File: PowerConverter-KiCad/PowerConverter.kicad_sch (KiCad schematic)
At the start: 47 parts, among them Q1 Q_NMOS_GDS, U1 UCC27517AQDBVRQ1, U2 STM32G431RBTx, U3 AP63205WU, U4 AMS1117-3.3, Y1 16MHz

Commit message: Şema ve BOM optimizasyonu tamamlandı. PCB Layout aşamasına geçiliyor.
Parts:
- removed D1: MBR1045, MBR1045CadModel:TO508P1050X476X2020-2, symbol MBR1045:MBR1045
- removed Q1: Q_NMOS_GDS, symbol Transistor_FET:Q_NMOS_GDS
- added C26, C28: 100nF, Capacitor_SMD:C_0603_1608Metric_Pad1.08x0.95mm_HandSolder, symbol Device:C
- added C27: 10uF, Capacitor_SMD:C_0805_2012Metric_Pad1.18x1.45mm_HandSolder, symbol Device:C
- added D1: PMEG060V100EPDZ, symbol Device:D_Schottky
- added Q1: IRFB7430PBF, symbol Simulation_SPICE:NMOS
- added R10: 10k, Resistor_SMD:R_0603_1608Metric_Pad0.98x0.95mm_HandSolder, symbol Device:R_US
- added TH1: Thermistor_NTC, Resistor_SMD:R_0603_1608Metric_Pad0.98x0.95mm_HandSolder, symbol Device:Thermistor_NTC
- C1: footprint (none) -> Capacitor_THT:CP_Radial_D16.0mm_P7.50mm
- C10, C14, C15, C16, C17, C21, C22, C23, C24, C25, C6, C7, C8: footprint (none) -> Capacitor_SMD:C_0603_1608Metric_Pad1.08x0.95mm_HandSolder
- C11, C12, C2, C9: footprint (none) -> Capacitor_SMD:C_1210_3225Metric_Pad1.33x2.70mm_HandSolder
- C13: footprint (none) -> Capacitor_Tantalum_SMD:CP_EIA-3528-21_Kemet-B_HandSolder
- C18, C19, C20, C4, C5: footprint (none) -> Capacitor_SMD:C_0805_2012Metric_Pad1.18x1.45mm_HandSolder
- C3: footprint (none) -> Capacitor_THT:CP_Radial_D8.0mm_P5.00mm
- D2: footprint (none) -> LED_SMD:LED_0805_2012Metric_Pad1.15x1.40mm_HandSolder
- L1, L2: value 47uH -> 10uH; footprint (none) -> Inductor_SMD:L_Bourns_SRP1245A
- L3: footprint (none) -> Inductor_SMD:L_Taiyo-Yuden_NR-30xx
- R1, R2, R4, R5, R7, R8, R9: footprint (none) -> Resistor_SMD:R_0603_1608Metric_Pad0.98x0.95mm_HandSolder
- R3: footprint (none) -> Resistor_SMD:R_2512_6332Metric_Pad1.40x3.35mm_HandSolder
- R6: footprint (none) -> Resistor_SMD:R_0805_2012Metric_Pad1.20x1.40mm_HandSolder
- U1: footprint DBV5_TEX -> footprints:DBV5_TEX
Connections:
- net +12V: now also C27.1, C28.1
- net +3.3V: now also R10.2
- net GND: now also C27.2, C28.2; no longer C5.2, C6.2, U1.2 (GND), U1.4 (IN-)
- net GNDA: now also C26.2, TH1.2
- net Gate: now also Q1.2 (G)
- net at C2.1, L1.2: now also Q1.1 (D)
- net Source: now reaches R3.1, R5.1
- net Source: now also C5.2, C6.2, U1.2 (GND), U1.4 (IN-), Q1.3 (S)
- net at C3.1, C4.1, R1.2: now also D1.1 (K)
- net at C2.2, L2.1: now also D1.2 (A)
- net PB2: now reaches U2.26 (PB2)
- net PB2: now also C26.1, R10.1, TH1.1
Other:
- moved on the sheet: C1, L1

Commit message: Layout: Buck ve LDO yerleşimi tamamlandı, sakin ada stratejisi uygulandı
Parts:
- added J1: 3220-10-0100-00, digikey-footprints:PinHeader_2x5_P1.27mm_Drill.7mm, symbol dk_Rectangular-Connectors-Headers-Male-Pins:3220-10-0100-00
- added J2: Conn_01x03_Pin, Connector_PinHeader_2.54mm:PinHeader_1x03_P2.54mm_Vertical, symbol Connector:Conn_01x03_Pin
- added R11: 10k, Resistor_SMD:R_0603_1608Metric_Pad0.98x0.95mm_HandSolder, symbol Device:R_US
- D1: footprint (none) -> Package_TO_SOT_SMD:TO-277B
- Q1: footprint (none) -> Package_TO_SOT_THT:TO-220-3_Vertical
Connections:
- net +3.3V: now also J1.1, J2.1 (Pin_1)
- net GND: now also J1.3, J1.5, J1.9, J2.3 (Pin_3); no longer R9.1
- net SWDCLK: now also J1.4
- net SWDIO: now also J1.2
- net V_O2: now reaches C3.1, C4.1, D1.1 (K), R1.2
- net V_O1: now reaches C2.2, D1.2 (A), L2.1
- net SW_NODE: now reaches C2.1, L1.2, Q1.1 (D)
- net BOOT0: now reaches R9.2, U2.61 (PB8)
- net at C24.2: now also R11.1; no longer U2.7 (PG10)
- net SWO: now reaches U2.56 (PB3)
- net SWO: now also J1.6
- new net: J2.2 (Pin_2), R9.1
- new net NRST: J1.10, R11.2, U2.7 (PG10)
- no-connect marks 0 -> 43
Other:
- note added: "STM32G4 serisinde bu jumper'ın çalışması için bir kereliğine yazılımsal bir ayar gerekebilir: nBOOT_SEL: Eğer Option Bytes içinde bu bit 1 ise, işlemci fiziksel BOOT0 pinini (senin bu jumper'ı) görmezden gelir. Çözüm: CubeIDE içindeki Programmer kısmından nBOOT_SEL bitini 0 yaparsan, işlemci artık tamamen senin bu fiziksel jumper'ının sözünü dinlemeye başlar."
- moved on the sheet: C24, C25

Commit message: SEPIC v2.0: 4-Layer Stackup, 12V Power Plane on In2, and High Current Via Stitching implemented
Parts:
- added D3, D4, D5, D6: BAT54S, Package_TO_SOT_SMD:SOT-23, symbol Diode:BAT54S
- added D7: SMAJ15A, Diode_SMD:D_SMC, symbol Diode:SMAJ15A
- added F1: Fuse, Fuse:Fuseholder_Cylinder-5x20mm_Wuerth_696103101002-SMD_Horizontal_Open, symbol Device:Fuse
- added H1, H2, H3, H4: MountingHole, MountingHole:MountingHole_3.2mm_M3, symbol Mechanical:MountingHole
- added J3, J4: Screw_Terminal_01x02, digikey-footprints:Term_Block_1x2_P5.08MM, symbol Connector:Screw_Terminal_01x02
- added R12, R13: 1k, Resistor_SMD:R_0603_1608Metric_Pad0.98x0.95mm_HandSolder, symbol Device:R_US
- R5: value 100 -> 1k
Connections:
- net +12V: now also F1.1, J3.2 (Pin_2); no longer C1.1, C27.1, C28.1, L1.1
- net +3.3VA: now also D3.2 (K), D4.2 (K), D5.2 (K), D6.2 (K)
- net GND: now also D7.2 (A2), J3.1 (Pin_1), J4.2 (Pin_2), R12.1
- net GNDA: now also D3.1 (A), D4.1 (A), D5.1 (A), D6.1 (A); no longer C8.2
- net PA1: now also D3.3 (COM)
- net PA7: now also D4.3 (COM); no longer C8.1, R5.2, U2.21 (PA7)
- net PB2: now also D5.3 (COM), R13.1; no longer C26.1, R10.1, TH1.1
- net V_O2: now also J4.1 (Pin_1)
- net I_SENSE_N: now reaches U2.19 (PA5)
- net I_SENSE_N: now also C8.2, R12.2
- new net: C26.1, R10.1, R13.2, TH1.1
- new net: C1.1, C27.1, C28.1, D7.1 (A1), F1.2, L1.1
- new net I_SENSE_P: C8.1, R5.2, U2.21 (PA7)
- new net PA5: D6.3 (COM)
- no-connect marks 43 -> 42
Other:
- moved on the sheet: C1, C2, C27, C28, C3, C4, C7, C8, D1, L1, L2, Q1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

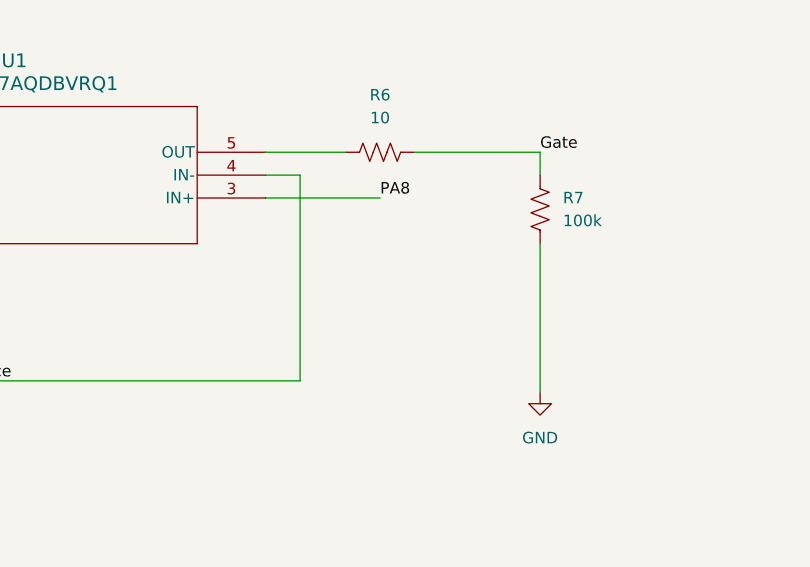
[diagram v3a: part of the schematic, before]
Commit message: Layout update: PA8 bottom layer shielding, U1 RC filter optimization, VDDA daisy-chain routing, and via-in-pad corrections
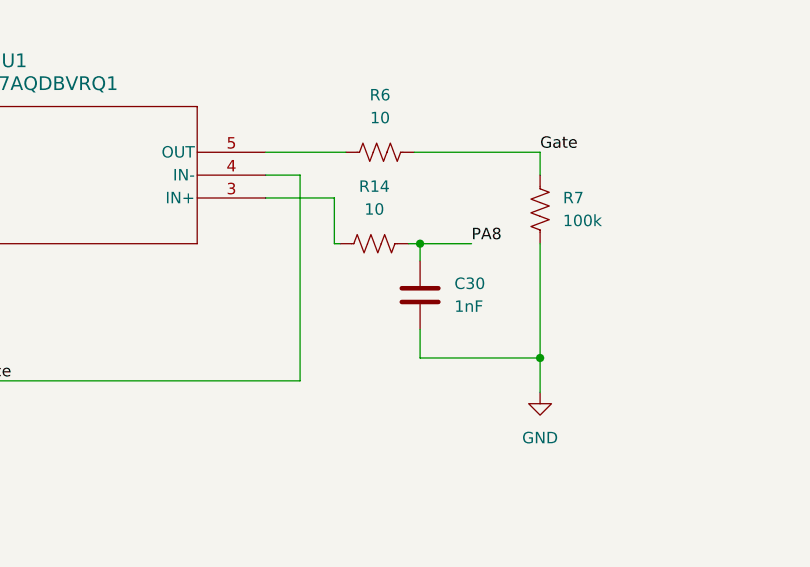
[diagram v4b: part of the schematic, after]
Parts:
- added C30: 1nF, Capacitor_SMD:C_0603_1608Metric_Pad1.08x0.95mm_HandSolder, symbol Device:C
- added R14: 10, Resistor_SMD:R_0805_2012Metric_Pad1.20x1.40mm_HandSolder, symbol Device:R_US
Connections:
- net GND: now also C30.2
- net PA8: now also C30.1, R14.2; no longer U1.3 (IN+)
- new net: R14.1, U1.3 (IN+)
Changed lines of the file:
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@@
 	)
 	(junction
+		(at 412.75 154.94)
+		(diameter 0)
+		(color 0 0 0 0)
+	)
+	(junction
 		(at 76.2 29.21)
 		(diameter 0)
@@
 	)
 	(junction
+		(at 399.415 142.24)
+		(diameter 0)
+		(color 0 0 0 0)
+	)
+	(junction
 		(at 334.01 50.8)
 		(diameter 0)
@@
 	(wire
 		(pts
-			(xy 412.75 142.24) (xy 412.75 158.75)
+			(xy 412.75 142.24) (xy 412.75 154.94)
 		)
 		(stroke
@@
 	(wire
 		(pts
+			(xy 389.89 137.16) (xy 382.27 137.16)
+		)
+		(stroke
+			(width 0)
+			(type default)
+		)
+	)
+	(wire
+		(pts
 			(xy 393.7 91.44) (xy 383.54 91.44)
 		)
@@
 	(wire
 		(pts
+			(xy 389.89 142.24) (xy 389.89 137.16)
+		)
+		(stroke
+			(width 0)
+			(type default)
+		)
+	)
+	(wire
+		(pts
 			(xy 370.84 74.93) (xy 370.84 78.74)
 		)
@@
 	(wire
 		(pts
+			(xy 412.75 154.94) (xy 412.75 158.75)
+		)
+		(stroke
+			(width 0)
+			(type default)
+		)
+	)
+	(wire
+		(pts
 			(xy 389.89 62.23) (xy 389.89 66.04)
 		)
@@
 	(wire
 		(pts
+			(xy 398.145 142.24) (xy 399.415 142.24)
+		)
+		(stroke
+			(width 0)
+			(type default)
+		)
+	)
+	(wire
+		(pts
 			(xy 448.31 34.29) (xy 448.31 36.83)
 		)
@@
 	(wire
 		(pts
+			(xy 399.415 151.765) (xy 399.415 154.94)
+		)
+		(stroke
+			(width 0)
+			(type default)
+		)
+	)
+	(wire
+		(pts
 			(xy 34.29 67.31) (xy 34.29 76.2)
 		)
@@
 	(wire
 		(pts
-			(xy 382.27 137.16) (xy 394.97 137.16)
+			(xy 389.89 142.24) (xy 390.525 142.24)
 		)
 		(stroke
@@
 	(wire
 		(pts
+			(xy 399.415 154.94) (xy 412.75 154.94)
+		)
+		(stroke
+			(width 0)
+			(type default)
+		)
+	)
+	(wire
+		(pts
 			(xy 95.25 72.39) (xy 87.63 72.39)
 		)
@@
 	(wire
 		(pts
+			(xy 399.415 142.24) (xy 399.415 144.145)
+		)
+		(stroke
+			(width 0)
+			(type default)
+		)
+	)
+	(wire
+		(pts
 			(xy 186.69 102.87) (xy 193.04 102.87)
 		)
@@
 	(wire
 		(pts
+			(xy 399.415 142.24) (xy 405.13 142.24)
+		)
+		(stroke
+			(width 0)
+			(type default)
+		)
+	)
+	(wire
+		(pts
 			(xy 539.75 38.1) (xy 511.81 38.1)
 		)
@@
 	)
 	(label "PA8"
-		(at 394.97 137.16 0)
+		(at 405.13 142.24 0)
 		(effects
 			(font
@@
 	)
 	(symbol
+		(lib_id "Device:R_US")
+		(at 394.335 142.24 90)
+		(unit 1)
+		(exclude_from_sim no)
+		(in_bom yes)
+		(on_board yes)
+		(dnp no)
+		(fields_autoplaced yes)
+		(property "Reference" "R14"
+			(at 394.335 135.89 90)
+			(effects
+				(font
+					(size 1.27 1.27)
+				)
+			)
+		)
+		(property "Value" "10"
+			(at 394.335 138.43 90)
+			(effects
+				(font
+					(size 1.27 1.27)
+				)
+			)
+		)
+		(property "Footprint" "Resistor_SMD:R_0805_2012Metric_Pad1.20x1.40mm_HandSolder"
+			(at 394.589 141.224 90)
+			(effects
+				(font
+					(size 1.27 1.27)
+				)
+				(hide yes)
+			)
+		)
+		(property "Datasheet" "~"
+			(at 394.335 142.24 0)
+			(effects
+				(font
+					(size 1.27 1.27)
+				)
+				(hide yes)
+			)
+		)
+		(property "Description" "Resistor, US symbol"
+			(at 394.335 142.24 0)
+			(effects
+				(font
+					(size 1.27 1.27)
+				)
+				(hide yes)
+			)
+		)
+		(pin "2"
+		)
+		(pin "1"
+		)
+		(instances
+			(project "PowerConverter"
+				(path "/fc5ddd0b-ae3d-43a4-b6e4-2a7ae79d729f"
+					(reference "R14")
+					(unit 1)
+				)
+			)
+		)
+	)
+	(symbol
 		(lib_id "Diode:BAT54S")
 		(at 760.73 30.48 0)
@@
 					(unit 1)
 				)
+			)
+		)
+	)
+	(symbol
+		(lib_id "Device:C")
+		(at 399.415 147.955 0)
+		(unit 1)
+		(exclude_from_sim no)
+		(in_bom yes)
+		(on_board yes)
+		(dnp no)
+		(fields_autoplaced yes)
+		(property "Reference" "C30"
+			(at 403.225 146.6849 0)
+			(effects
+				(font
+					(size 1.27 1.27)
+				)
+				(justify left)
+			)
+		)
+		(property "Value" "1nF"
+			(at 403.225 149.2249 0)
+			(effects
+				(font
+					(size 1.27 1.27)
+				)
+				(justify left)
+			)
+		)
+		(property "Footprint" "Capacitor_SMD:C_0603_1608Metric_Pad1.08x0.95mm_HandSolder"
+			(at 400.3802 151.765 0)
+			(effects
+				(font
+					(size 1.27 1.27)
+				)
+				(hide yes)
+			)
+		)
+		(property "Datasheet" "~"
+			(at 399.415 147.955 0)
+			(effects
+				(font
+					(size 1.27 1.27)
+				)
+				(hide yes)
+			)
+		)
+		(property "Description" "Unpolarized capacitor"
+			(at 399.415 147.955 0)
+			(effects
+				(font
+					(size 1.27 1.27)
+				)
+				(hide yes)
+			)
+		)
+		(pin "1"
+		)
+		(pin "2"
+		)
+		(instances
+			(project "PowerConverter"
+				(path "/fc5ddd0b-ae3d-43a4-b6e4-2a7ae79d729f"
+					(reference "C30")
+					(unit 1)
+				)
